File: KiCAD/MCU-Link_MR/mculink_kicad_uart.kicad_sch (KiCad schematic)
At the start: 11 parts, among them J11 JST-GH_BM06B, U10 SN74LVC1T45GW, U9 SN74LVC1T45GW

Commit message: completed BOM
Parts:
- C40, C41, C42, C43: value 100n -> 100nF 6.3V; mouser# (none) -> 80-C0603C104K9R
- D4: value PESD5V0L5UV -> PESD5V0L5UV,115; mouser# (none) -> 771-PESD5V0L5UV115
- J11: value JST-GH_BM06B -> JST-GH BM06B-GHS; MFR# (none) -> BM06B-GHS-TBT; digikey# (none) -> 455-BM06B-GHS-TBTCT-ND
- R26, R27: value 10R -> 10R 5% 100mW; mouser# (none) -> 652-CR0603-JW-100ELF
- R28: value 100k -> 100k 5% 100mW; mouser# (none) -> 652-CR0603-JW-104ELF
- U10, U9: value SN74LVC1T45GW -> 74LVC1T45GW; mouser# (none) -> 771-74LVC1T45GWQ100H

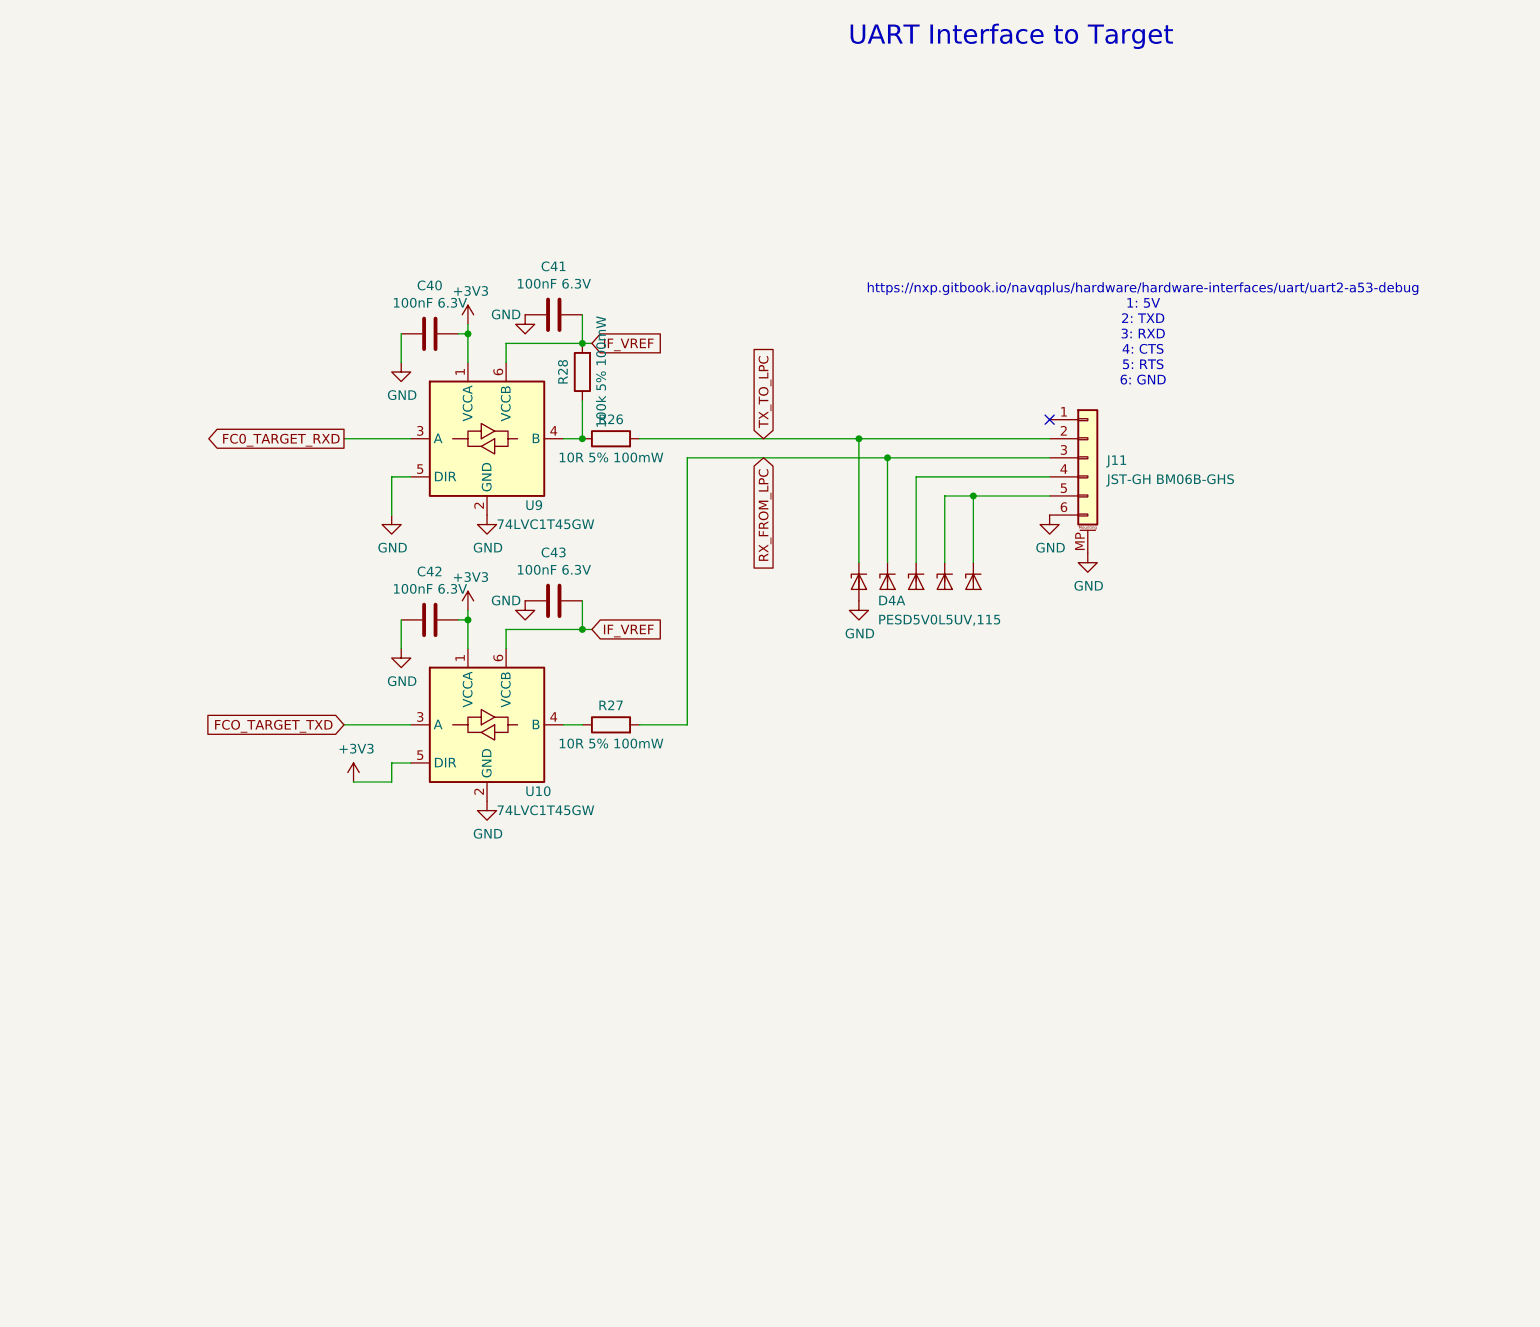
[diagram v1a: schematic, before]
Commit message: updates for v0.3: added RTS/CTS signals for J11
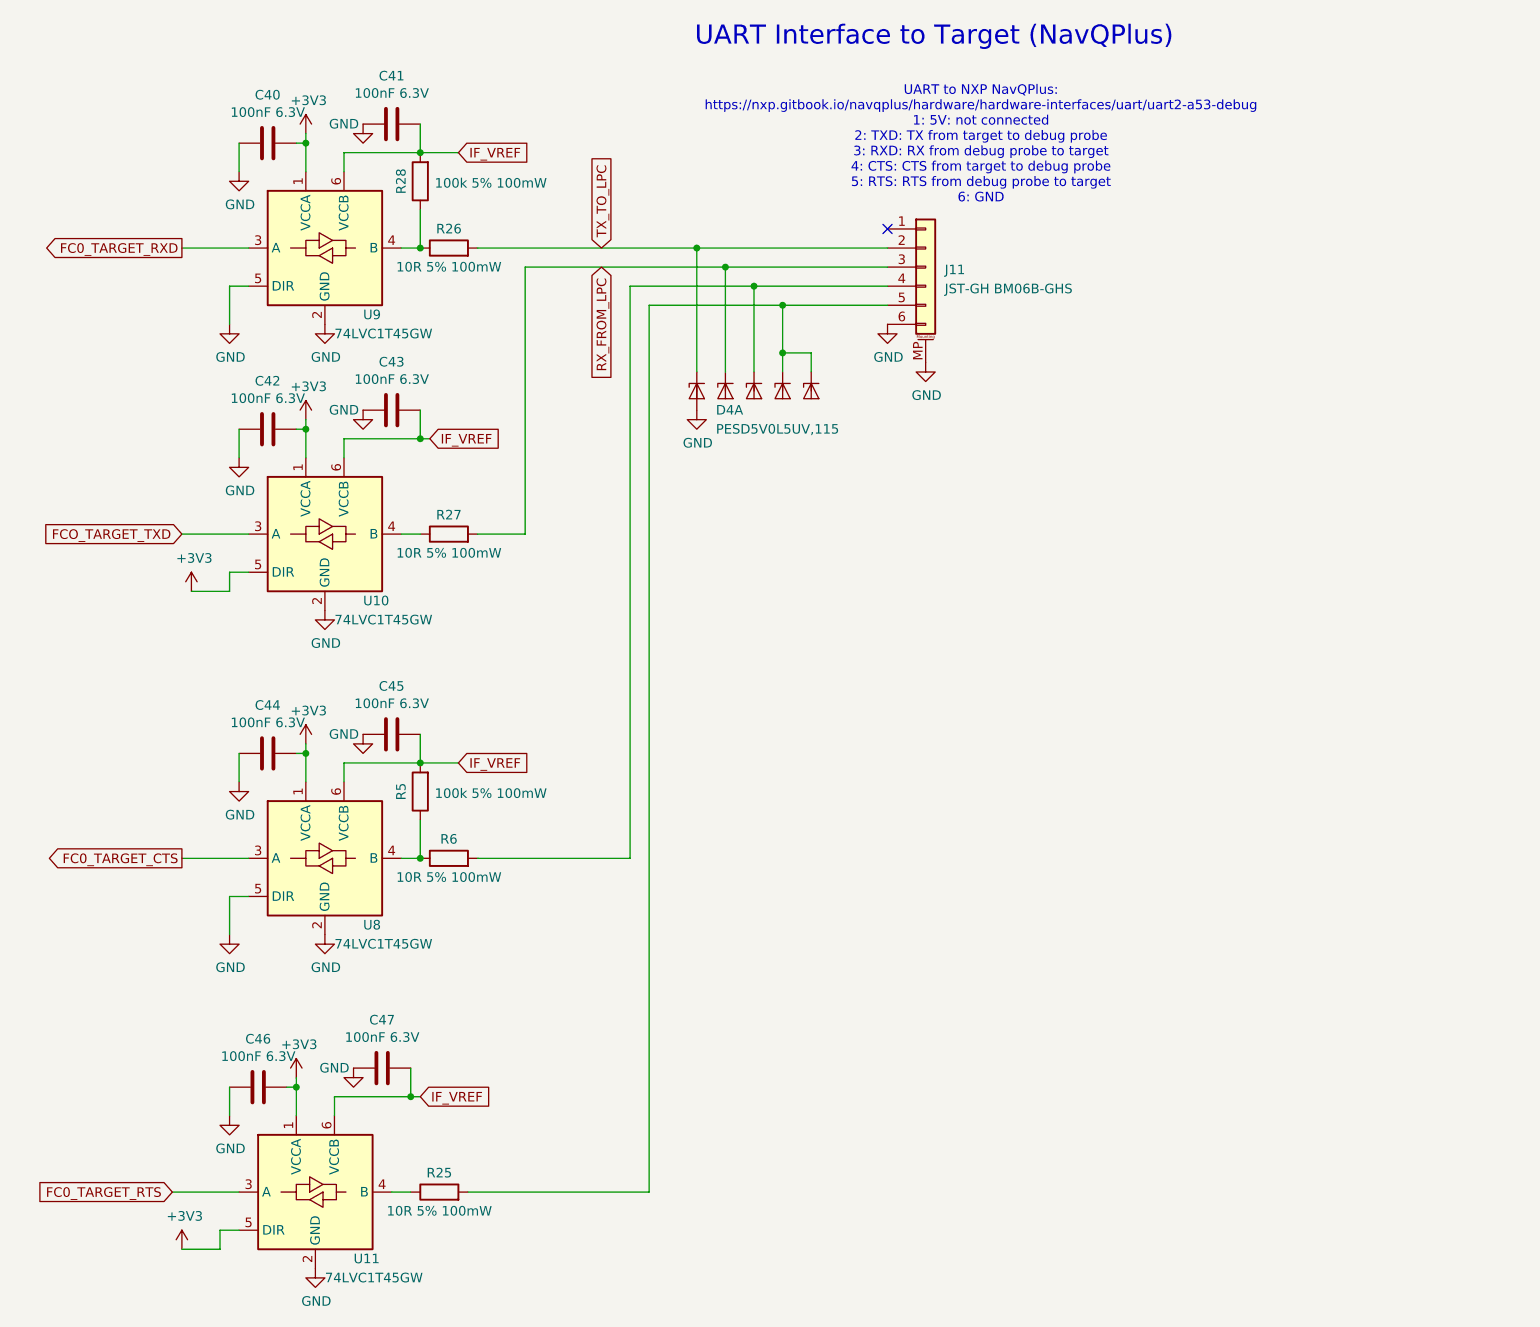
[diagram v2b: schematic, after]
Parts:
- added C44, C45, C46, C47: 100nF 6.3V, Capacitor_SMD:C_0402_1005Metric, symbol Device:C
- added R25, R6: 10R 5% 100mW, Resistor_SMD:R_0402_1005Metric, symbol Device:R
- added R5: 100k 5% 100mW, Resistor_SMD:R_0402_1005Metric, symbol Device:R
- added U11, U8: 74LVC1T45GW, Package_TO_SOT_SMD:SOT-363_SC-70-6, symbol mculink_kicad:SN74LVC1T45GW
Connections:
- net +3V3: now also C44.2, C46.2, U11.1 (VCCA), U11.5 (DIR), U8.1 (VCCA)
- net GND: now also C44.1, C45.1, C46.1, C47.1, U11.2 (GND), U8.2 (GND), U8.5 (DIR)
- net IF_VREF: now also C45.2, C47.2, R5.2, U11.6 (VCCB), U8.6 (VCCB)
- net at D4.4 (K3), J11.4 (Pin_4): now also R6.2
- net at D4.5 (K4), D4.6 (K5), J11.5 (Pin_5): now also R25.2
- new net: R25.1, U11.4 (B)
- new net: R5.1, R6.1, U8.4 (B)
- new net FC0_TARGET_CTS: U8.3 (A)
- new net FC0_TARGET_RTS: U11.3 (A)
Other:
- note added: "UART Interface to Target (NavQPlus)"
- note added: "UART to NXP NavQPlus: https://nxp.gitbook.io/navqplus/hardware/hardware-interfaces/uart/uart2-a53-debug 1: 5V: not connected 2: TXD: TX from target to debug probe 3: RXD: RX from debug probe to target 4: CTS: CTS from target to debug probe 5: RTS: RTS from debug probe to target 6: GND"
- note removed: "UART Interface to Target"
- note removed: "https://nxp.gitbook.io/navqplus/hardware/hardware-interfaces/uart/uart2-a53-debug 1: 5V 2: TXD 3: RXD 4: CTS 5: RTS 6: GND"
- moved on the sheet: C40, C41, C42, C43, D4A, J11, R26, R27, R28, U10, U9

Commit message: updated BOM part numbers for v0.3
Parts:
- R25, R6: mouser# 652-CR0603-JW-100ELF -> 667-ERJ-2GEJ100X
- R5: mouser# 652-CR0603-JW-104ELF -> 791-MR04X104JTL
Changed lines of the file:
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@@
 			)
 		)
-		(property "mouser#" "652-CR0603-JW-104ELF"
+		(property "mouser#" "791-MR04X104JTL"
 			(at 67.31 120.65 0)
 			(effects
@@
 			)
 		)
-		(property "mouser#" "652-CR0603-JW-100ELF"
+		(property "mouser#" "667-ERJ-2GEJ100X "
 			(at 71.12 129.54 0)
 			(effects
@@
 			)
 		)
-		(property "mouser#" "652-CR0603-JW-100ELF"
+		(property "mouser#" "667-ERJ-2GEJ100X "
 			(at 69.85 173.99 0)
 			(effects

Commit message: new v0.4 with pull-down for cts signal (instead pull-up)
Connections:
- net GND: now also R5.1
- net IF_VREF: no longer R5.2
- net at R6.1, U8.4 (B): now also R5.2; no longer R5.1
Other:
- moved on the sheet: R5, R6
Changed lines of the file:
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@@
 	)
 	(junction
-		(at 67.31 129.54)
+		(at 111.76 53.34)
 		(diameter 0)
 		(color 0 0 0 0)
 	)
 	(junction
-		(at 111.76 53.34)
+		(at 66.04 161.29)
 		(diameter 0)
 		(color 0 0 0 0)
 	)
 	(junction
-		(at 66.04 161.29)
+		(at 74.93 129.54)
 		(diameter 0)
 		(color 0 0 0 0)
@@
 	(wire
 		(pts
-			(xy 64.77 129.54) (xy 67.31 129.54)
+			(xy 64.77 129.54) (xy 74.93 129.54)
 		)
 		(stroke
@@
 	(wire
 		(pts
+			(xy 74.93 129.54) (xy 74.93 134.62)
+		)
+		(stroke
+			(width 0)
+			(type default)
+		)
+	)
+	(wire
+		(pts
 			(xy 111.76 53.34) (xy 111.76 64.77)
 		)
@@
 	(wire
 		(pts
-			(xy 66.04 161.29) (xy 66.04 157.48)
+			(xy 87.63 129.54) (xy 95.25 129.54)
 		)
 		(stroke
@@
 	(wire
 		(pts
-			(xy 107.95 50.8) (xy 107.95 64.77)
+			(xy 66.04 161.29) (xy 66.04 157.48)
 		)
 		(stroke
@@
 	(wire
 		(pts
-			(xy 129.54 53.34) (xy 111.76 53.34)
+			(xy 107.95 50.8) (xy 107.95 64.77)
 		)
 		(stroke
@@
 	(wire
 		(pts
-			(xy 57.15 119.38) (xy 57.15 116.84)
+			(xy 129.54 53.34) (xy 111.76 53.34)
 		)
 		(stroke
@@
 	(wire
 		(pts
-			(xy 67.31 116.84) (xy 72.39 116.84)
+			(xy 57.15 119.38) (xy 57.15 116.84)
 		)
 		(stroke
@@
 	(wire
 		(pts
-			(xy 50.8 72.39) (xy 52.07 72.39)
+			(xy 67.31 116.84) (xy 72.39 116.84)
 		)
 		(stroke
@@
 	(wire
 		(pts
-			(xy 95.25 129.54) (xy 74.93 129.54)
+			(xy 50.8 72.39) (xy 52.07 72.39)
 		)
 		(stroke
@@
 	(wire
 		(pts
+			(xy 74.93 129.54) (xy 80.01 129.54)
+		)
+		(stroke
+			(width 0)
+			(type default)
+		)
+	)
+	(wire
+		(pts
 			(xy 41.91 134.62) (xy 44.45 134.62)
 		)
@@
 	(wire
 		(pts
-			(xy 67.31 129.54) (xy 67.31 124.46)
-		)
-		(stroke
-			(width 0)
-			(type default)
-		)
-	)
-	(wire
-		(pts
 			(xy 41.91 53.34) (xy 44.45 53.34)
 		)
@@
 		)
 		(property "Value" "100nF 6.3V"
-			(at 46.99 30.2006 90)
+			(at 43.18 30.226 90)
 			(effects
 				(font
@@
 		)
 		(property "Value" "100nF 6.3V"
-			(at 46.99 68.3006 90)
+			(at 43.18 68.326 90)
 			(effects
 				(font
@@
 	)
 	(symbol
+		(lib_id "power:GND")
+		(at 74.93 142.24 0)
+		(unit 1)
+		(exclude_from_sim no)
+		(in_bom yes)
+		(on_board yes)
+		(dnp no)
+		(property "Reference" "#PWR0113"
+			(at 74.93 148.59 0)
+			(effects
+				(font
+					(size 1.27 1.27)
+				)
+				(hide yes)
+			)
+		)
+		(property "Value" "GND"
+			(at 75.057 146.6342 0)
+			(effects
+				(font
+					(size 1.27 1.27)
+				)
+			)
+		)
+		(property "Footprint" ""
+			(at 74.93 142.24 0)
+			(effects
+				(font
+					(size 1.27 1.27)
+				)
+				(hide yes)
+			)
+		)
+		(property "Datasheet" ""
+			(at 74.93 142.24 0)
+			(effects
+				(font
+					(size 1.27 1.27)
+				)
+				(hide yes)
+			)
+		)
+		(property "Description" "Power symbol creates a global label with name \"GND\" , ground"
+			(at 74.93 142.24 0)
+			(effects
+				(font
+					(size 1.27 1.27)
+				)
+				(hide yes)
+			)
+		)
+		(pin "1"
+		)
+		(instances
+			(project "MCU-Link_MR"
+				(path "/5d025764-753a-4b80-8d3d-c9a8a22c9527/00000000-0000-0000-0000-0000603d0055"
+					(reference "#PWR0113")
+					(unit 1)
+				)
+			)
+		)
+	)
+	(symbol
 		(lib_id "mculink_kicad:SN74LVC1T45GW")
 		(at 53.34 173.99 0)
@@
 	(symbol
 		(lib_id "Device:R")
-		(at 67.31 120.65 180)
+		(at 74.93 138.43 180)
 		(unit 1)
 		(exclude_from_sim no)
@@
 		(dnp no)
 		(property "Reference" "R5"
-			(at 64.77 120.65 90)
+			(at 72.39 138.43 90)
 			(effects
 				(font
@@
 		)
 		(property "Value" "100k 5% 100mW"
-			(at 76.708 120.904 0)
+			(at 84.328 138.684 0)
 			(effects
 				(font
@@
 		)
 		(property "Footprint" "Resistor_SMD:R_0402_1005Metric"
-			(at 69.088 120.65 90)
+			(at 76.708 138.43 90)
 			(effects
 				(font
@@
 		)
 		(property "Datasheet" "~"
-			(at 67.31 120.65 0)
+			(at 74.93 138.43 0)
 			(effects
 				(font
@@
 		)
 		(property "Description" "Resistor"
-			(at 67.31 120.65 0)
+			(at 74.93 138.43 0)
 			(effects
 				(font
@@
 		)
 		(property "distrelec#" ""
-			(at 67.31 120.65 0)
+			(at 74.93 138.43 0)
 			(effects
 				(font
@@
 		)
 		(property "digikey#" ""
-			(at 67.31 120.65 0)
+			(at 74.93 138.43 0)
 			(effects
 				(font
@@
 		)
 		(property "mouser#" "791-MR04X104JTL"
-			(at 67.31 120.65 0)
+			(at 74.93 138.43 0)
 			(effects
 				(font
@@
 	(symbol
 		(lib_id "Device:R")
-		(at 71.12 129.54 90)
+		(at 83.82 129.54 90)
 		(unit 1)
 		(exclude_from_sim no)
@@
 		(dnp no)
 		(property "Reference" "R6"
-			(at 71.12 127 90)
+			(at 83.82 127 90)
 			(effects
 				(font
@@
 		)
 		(property "Value" "10R 5% 100mW"
-			(at 71.12 132.08 90)
+			(at 83.82 132.08 90)
 			(effects
 				(font
@@
 		)
 		(property "Footprint" "Resistor_SMD:R_0402_1005Metric"
-			(at 71.12 131.318 90)
+			(at 83.82 131.318 90)
 			(effects
 				(font
@@
 		)
 		(property "Datasheet" "~"
-			(at 71.12 129.54 0)
+			(at 83.82 129.54 0)
 			(effects
 				(font
@@
 		)
 		(property "Description" "Resistor"
-			(at 71.12 129.54 0)
+			(at 83.82 129.54 0)
 			(effects
 				(font
@@
 		)
 		(property "distrelec#" ""
-			(at 71.12 129.54 0)
+			(at 83.82 129.54 0)
 			(effects
 				(font
@@
 		)
 		(property "digikey#" ""
-			(at 71.12 129.54 0)
+			(at 83.82 129.54 0)
 			(effects
 				(font
@@
 		)
 		(property "mouser#" "667-ERJ-2GEJ100X "
-			(at 71.12 129.54 0)
+			(at 83.82 129.54 0)
 			(effects
 				(font
@@
 		)
 		(property "Value" "100nF 6.3V"
-			(at 45.72 155.9306 90)
+			(at 41.91 155.956 90)
 			(effects
 				(font
@@
 		)
 		(property "Value" "100nF 6.3V"
-			(at 46.99 111.4806 90)
+			(at 43.18 111.506 90)
 			(effects
 				(font

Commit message: Replaced 0603 with 0402 footprints for C and R; removed designators; shifted components to the left
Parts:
- C40, C41, C42, C43: footprint Capacitor_SMD:C_0603_1608Metric -> Capacitor_SMD:C_0402_1005Metric
- R26, R27, R28: footprint Resistor_SMD:R_0603_1608Metric -> Resistor_SMD:R_0402_1005Metric
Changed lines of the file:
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@@
 			)
 		)
-		(property "Footprint" "Resistor_SMD:R_0603_1608Metric"
+		(property "Footprint" "Resistor_SMD:R_0402_1005Metric"
 			(at 69.088 39.37 90)
 			(effects
@@
 			)
 		)
-		(property "Footprint" "Capacitor_SMD:C_0603_1608Metric"
+		(property "Footprint" "Capacitor_SMD:C_0402_1005Metric"
 			(at 50.8 33.3248 0)
 			(effects
@@
 			)
 		)
-		(property "Footprint" "Capacitor_SMD:C_0603_1608Metric"
+		(property "Footprint" "Capacitor_SMD:C_0402_1005Metric"
 			(at 67.31 30.7848 0)
 			(effects
@@
 			)
 		)
-		(property "Footprint" "Resistor_SMD:R_0603_1608Metric"
+		(property "Footprint" "Resistor_SMD:R_0402_1005Metric"
 			(at 71.12 50.038 90)
 			(effects
@@
 			)
 		)
-		(property "Footprint" "Capacitor_SMD:C_0603_1608Metric"
+		(property "Footprint" "Capacitor_SMD:C_0402_1005Metric"
 			(at 50.8 71.4248 0)
 			(effects
@@
 			)
 		)
-		(property "Footprint" "Capacitor_SMD:C_0603_1608Metric"
+		(property "Footprint" "Capacitor_SMD:C_0402_1005Metric"
 			(at 67.31 68.8848 0)
 			(effects
@@
 			)
 		)
-		(property "Footprint" "Resistor_SMD:R_0603_1608Metric"
+		(property "Footprint" "Resistor_SMD:R_0402_1005Metric"
 			(at 71.12 88.138 90)
 			(effects
